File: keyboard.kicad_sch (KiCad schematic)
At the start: 23 parts, among them J2 Conn_01x05_Pin, SW1 SW_Push, U1 STM32F072C8Tx, U3 XC6206PxxxMR, U4 USB6B1

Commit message: BigBass recommended changes + more thanks
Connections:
- net D+: now also U4.2 (I/O1); no longer U4.3 (I/O2)
- net D-: now also U4.3 (I/O2); no longer U4.2 (I/O1)
- net DIn+: now also U4.7 (I/O1); no longer U4.6 (I/O2)
- net DIn-: now also U4.6 (I/O2); no longer U4.7 (I/O1)

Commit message: Big round of changes. Click to read more.
- Labels on the MCU have been switched around to make routing nicer
- ESD Chip is now right next to the connector
- All 3.3V inputs have the 100nF capacitor correctly placed next to it
    - VDDA has an extra 10uF capacitor (as per the STM32 spec sheet)
    - The start of the 3.3V rail has a 4.7uF capacitor (as per the STM32 spec sheet)
- All LEDs now have a 100nF capacitor connected to it, and a 100ohm resistor at the start of the data line
- LED data line has been level shifted to 5V
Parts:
- added C10: 100nF, Capacitor_SMD:C_0402_1005Metric, symbol Device:C
- added C119: 4.7uF, Capacitor_SMD:C_0603_1608Metric, symbol Device:C
- added R2: 470, Resistor_SMD:R_0402_1005Metric, symbol Device:R
- added U2: 74AHCT1G125, Package_SO:TSOP-5_1.65x3.05mm_P0.95mm, symbol 74xGxx:74AHCT1G125
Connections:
- net +3.3V: now also C119.1
- net +5V: now also C10.2, U2.5 (VCC)
- net Col01: now also U1.22 (PB11); no longer U1.39 (PB3)
- net Col02: now also U1.21 (PB10); no longer U1.40 (PB4)
- net Col03: now also U1.20 (PB2); no longer U1.41 (PB5)
- net Col04: now also U1.19 (PB1); no longer U1.42 (PB6)
- net Col05: now also U1.18 (PB0); no longer U1.43 (PB7)
- net Col06: now also U1.17 (PA7); no longer U1.45 (PB8)
- net Col07: now also U1.16 (PA6); no longer U1.46 (PB9)
- net Col08: now also U1.2 (PC13); no longer U1.21 (PB10)
- net Col09: now also U1.3 (PC14); no longer U1.22 (PB11)
- net Col10: now also U1.4 (PC15); no longer U1.25 (PB12)
- net Col11: now also U1.5 (PF0); no longer U1.26 (PB13)
- net Col12: now also U1.6 (PF1); no longer U1.27 (PB14)
- net Col13: now also U1.11 (PA1); no longer U1.28 (PB15)
- net Col14: now also U1.12 (PA2); no longer U1.10 (PA0)
- net Col15: now also U1.25 (PB12); no longer U1.11 (PA1)
- net Col16: now also U1.26 (PB13); no longer U1.12 (PA2)
- net Col17: now also U1.31 (PA10); no longer U1.13 (PA3)
- net Col18: now also U1.30 (PA9); no longer U1.14 (PA4)
- net Col19: now also U1.29 (PA8); no longer U1.15 (PA5)
- net Col20: now also U1.28 (PB15); no longer U1.16 (PA6)
- net Col21: now also U1.27 (PB14); no longer U1.17 (PA7)
- net D+: now also U1.32 (PA11), U4.3 (I/O2); no longer U1.33 (PA12), U4.2 (I/O1)
- net D-: now also U1.33 (PA12), U4.2 (I/O1); no longer U1.32 (PA11), U4.3 (I/O2)
- net DIn+: now also U4.6 (I/O2); no longer U4.7 (I/O1)
- net DIn-: now also U4.7 (I/O1); no longer U4.6 (I/O2)
- net GND: now also C10.1, C119.2, U2.1, U2.3 (GND)
- net LED: now also R2.2; no longer U1.29 (PA8)
- net Row1: now also U1.37 (PA14); no longer U1.2 (PC13)
- net Row2: now also U1.38 (PA15); no longer U1.3 (PC14)
- net Row3: now also U1.39 (PB3); no longer U1.4 (PC15)
- net Row4: now also U1.40 (PB4); no longer U1.18 (PB0)
- net Row5: now also U1.41 (PB5); no longer U1.19 (PB1)
- net Row6: now also U1.42 (PB6); no longer U1.20 (PB2)
- new net: R2.1, U2.4
- new net LED_DATA: U1.13 (PA3), U2.2
- no-connect marks 41 -> 40
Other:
- note added: "Each cap should be connected to the power inputs of the STM32 VDDA should have the 100nF and the 10uF The 4.7 uF should be connected between the start of the 3.3V rail and ground."
- note added: "This file contains the main board's USB connection, the MCU, and miscellaneous power components. The LEDs require 5V logic, but the STM32 outputs 3.3V, so we need the level shifter to adjust for that."
- note removed: "This file contains the main board's USB connection, the MCU, and miscellaneous power components"
- moved on the sheet: C2, C3, C4, C5, C6, C7, R1, R4, SW1

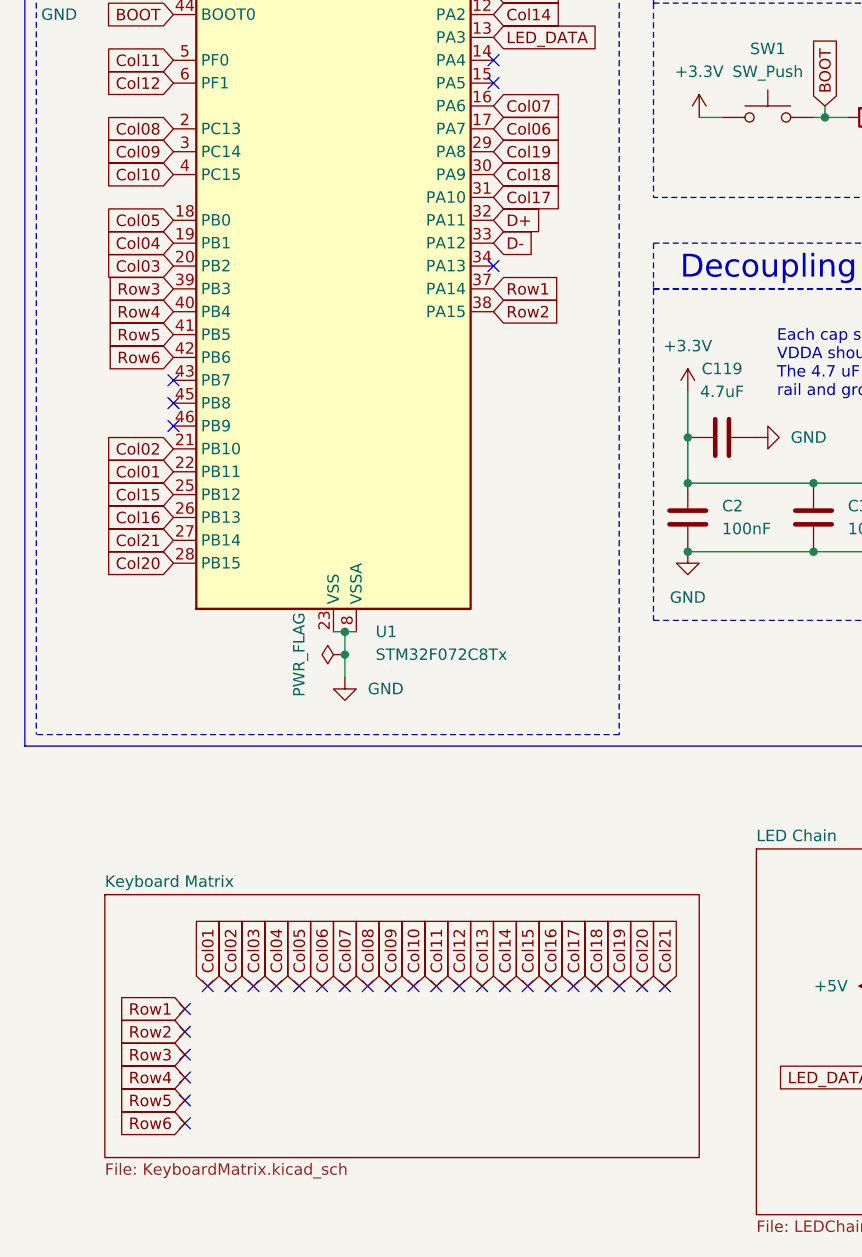
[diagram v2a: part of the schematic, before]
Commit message: Simplified key routing
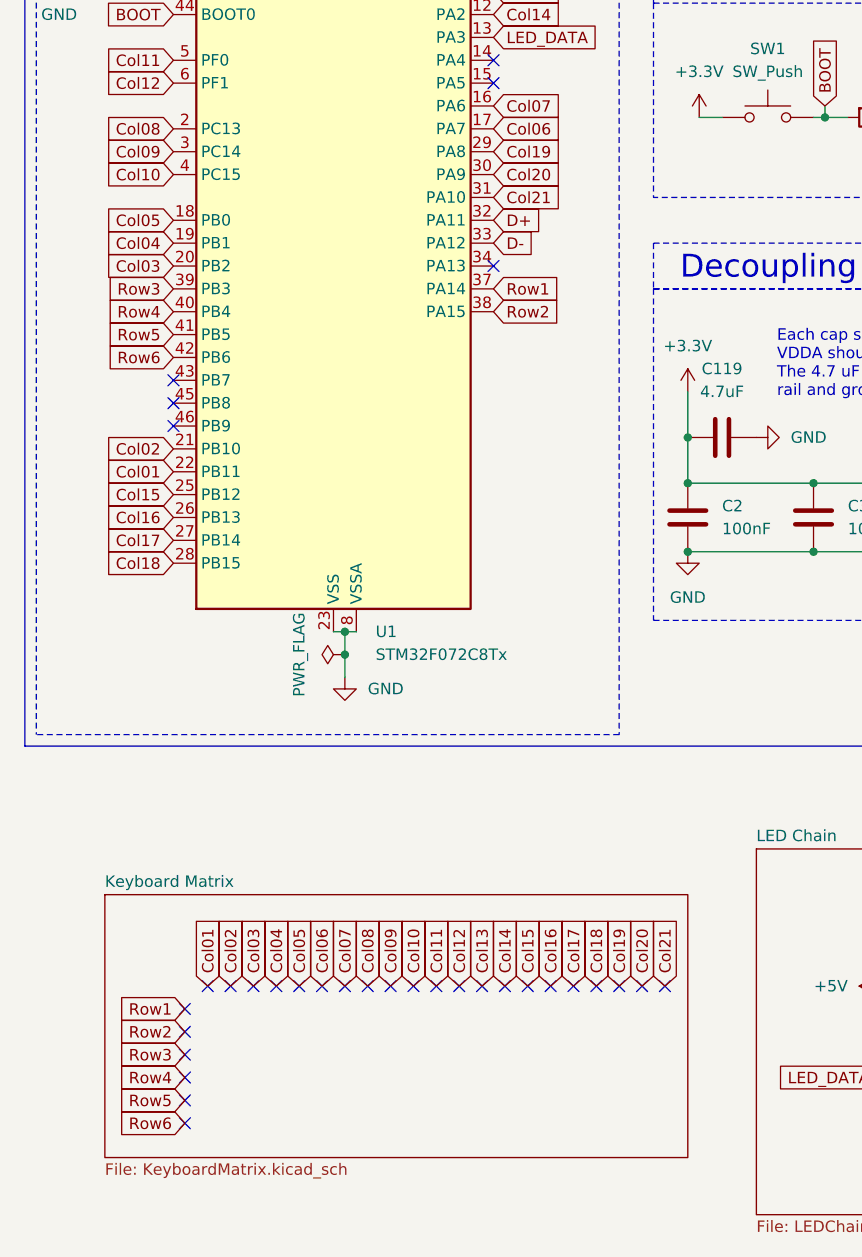
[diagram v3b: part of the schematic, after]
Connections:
- net Col17: now also U1.27 (PB14); no longer U1.31 (PA10)
- net Col18: now also U1.28 (PB15); no longer U1.30 (PA9)
- net Col20: now also U1.30 (PA9); no longer U1.28 (PB15)
- net Col21: now also U1.31 (PA10); no longer U1.27 (PB14)

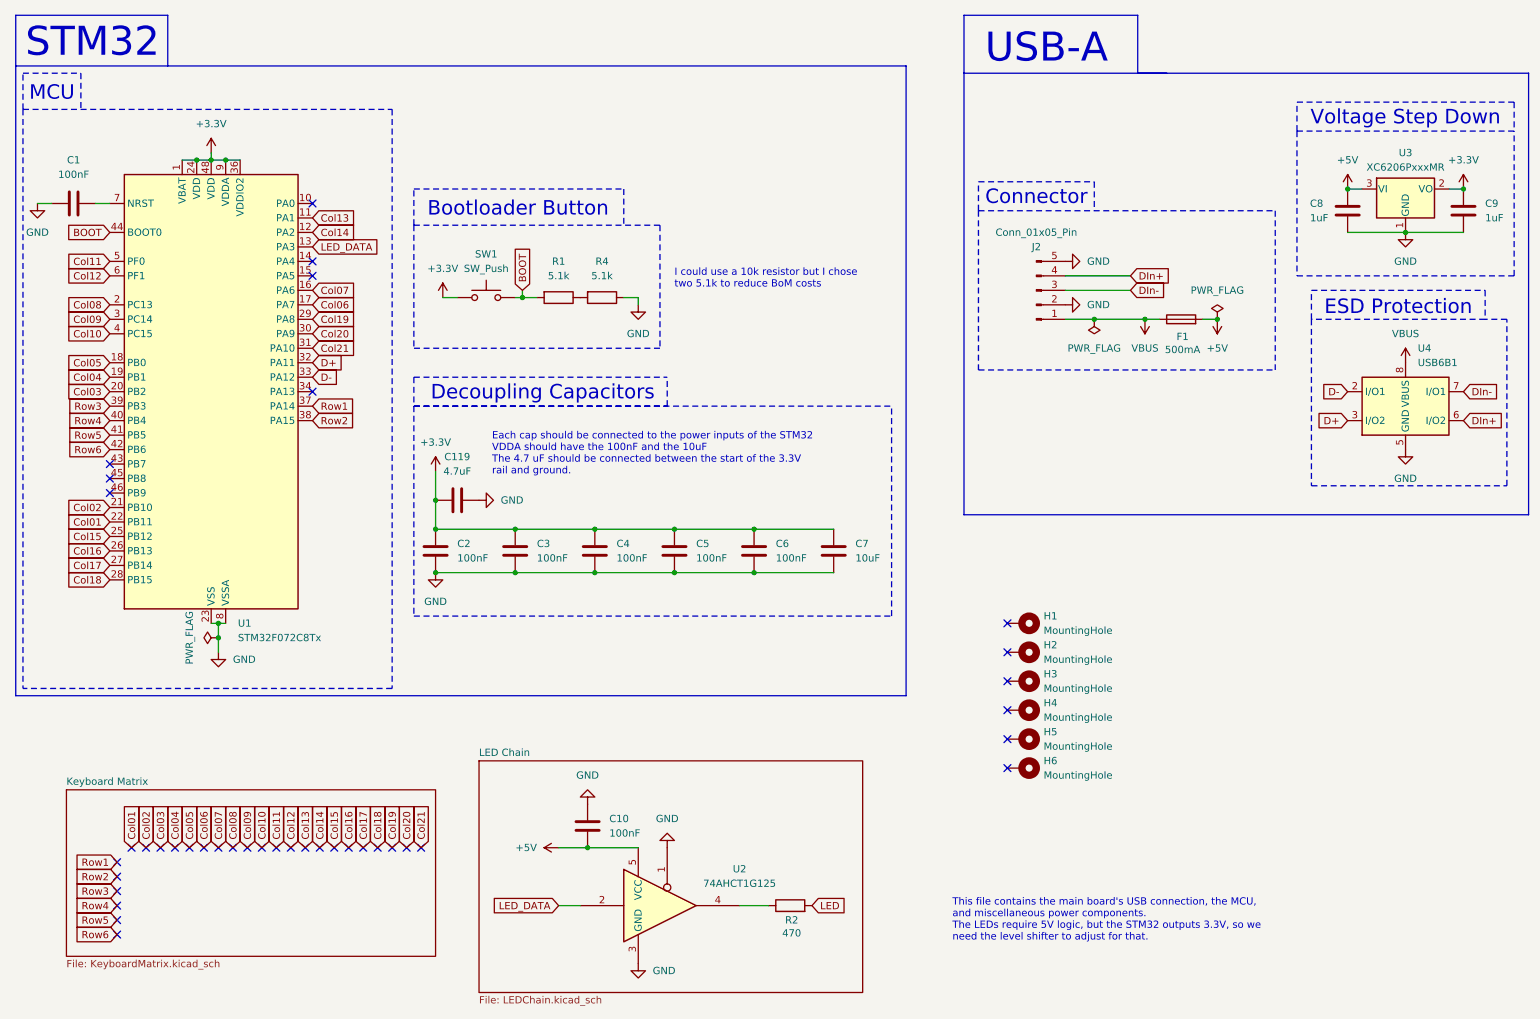
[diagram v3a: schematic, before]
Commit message: Keyboard wiring simplifcations + schematic editor warning fixes
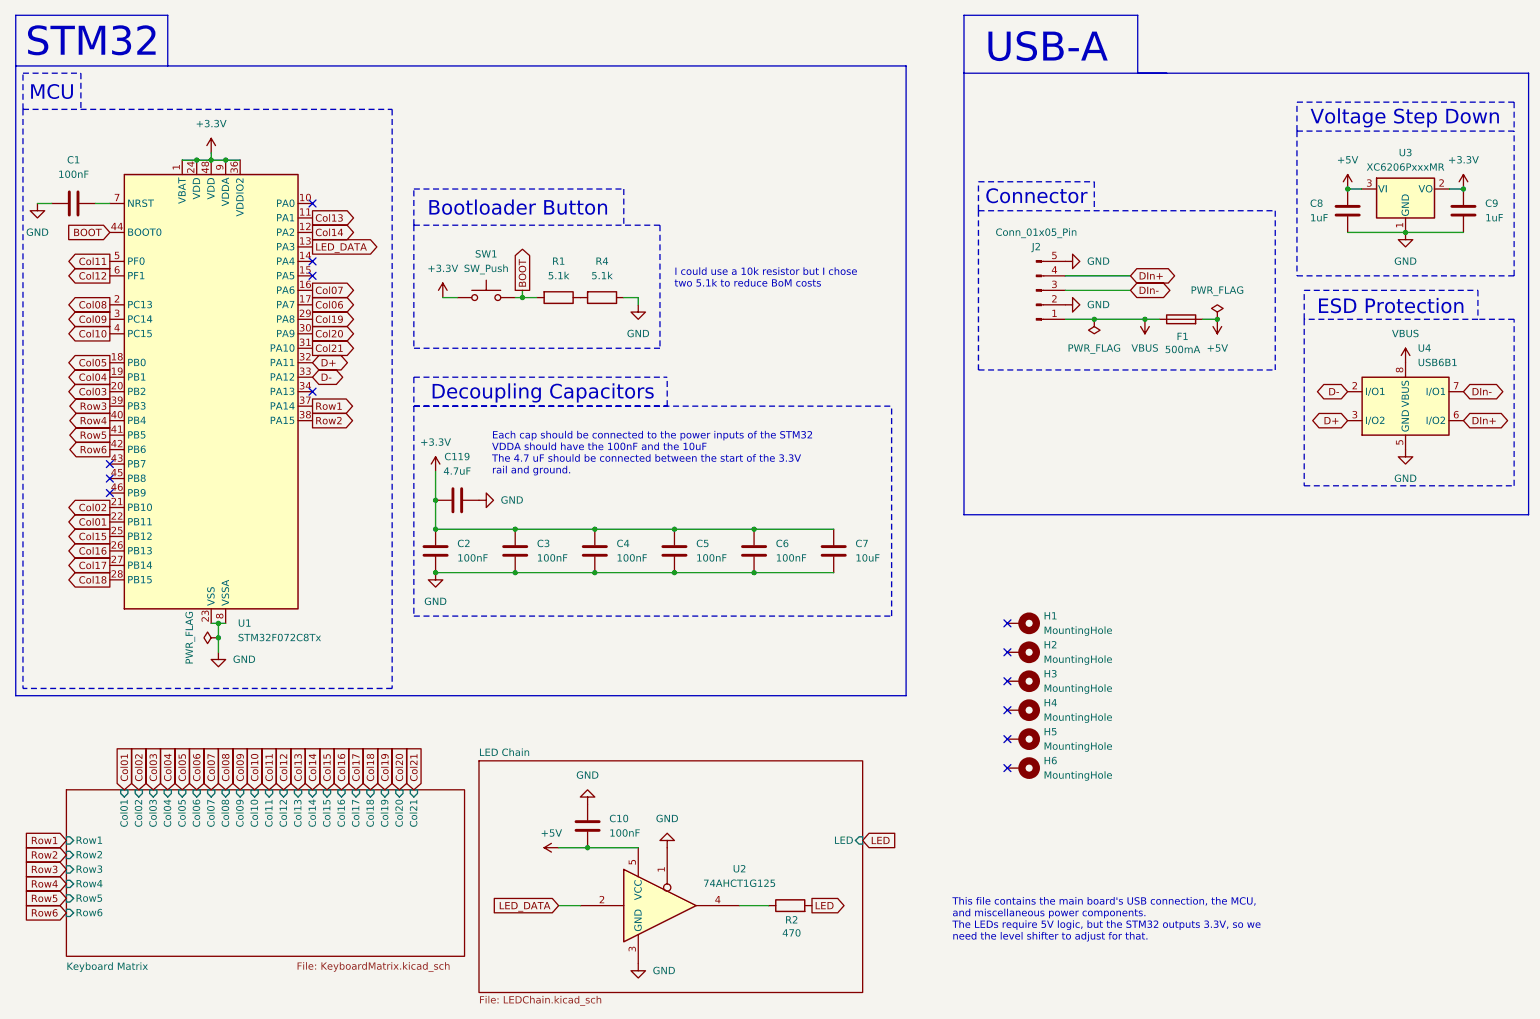
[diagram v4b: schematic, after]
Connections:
- no-connect marks 40 -> 13
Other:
- sheet Keyboard Matrix ports: added Col01, Col02, Col03, Col04, Col05, Col06, Col07, Col08, Col09, Col10, Col11, Col12, Col13, Col14, Col15, Col16, Col17, Col18, Col19, Col20, Col21, Row1, Row2, Row3, Row4, Row5, Row6; removed none
- sheet LED Chain ports: added LED; removed none
